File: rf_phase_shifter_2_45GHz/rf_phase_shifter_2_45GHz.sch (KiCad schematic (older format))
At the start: 12 parts, among them J1 Conn_Coaxial, J2 Conn_Coaxial, J3 Conn_Coaxial

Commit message: update
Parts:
- removed FL1: C2327J5003AHF, C2327J5003AHF, symbol RF:C2327J5003AHF
- added FL1: C2327J5003AHF, analog_rf_phase_shifter_module:C2327J5003AHF, symbol analog_rf_phase_shifter_module:C2327J5003AHF
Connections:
- net GND: now also FL1.2 (GND_1), FL1.5 (GND_2)
- net at D1.1 (K), D3.1 (K), L1.2: now also FL1.6 (COUPLED)
- net at D2.1 (K), D4.1 (K), L2.2: now also FL1.4 (DIRECT)
- net at C1.1: now also FL1.1 (INPUT)
- net at C2.2: now also FL1.3 (ISOLATED)
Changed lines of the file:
@@
 EELAYER 30 0
 EELAYER END
-$Descr A4 11693 8268
+$Descr User 8268 5827
 encoding utf-8
 Sheet 1 1
-Title ""
-Date ""
-Rev ""
-Comp ""
+Title "Analog RF phase shifter 2,4-2,5GHz"
+Date "2021-05-03"
+Rev "1.0.0"
+Comp "Marcin Wachowiak, Poland"
 Comment1 ""
 Comment2 ""
@@
 	4450 1950 4450 1900
 Connection ~ 3900 1900
-$Comp
-L RF:C2327J5003AHF FL1
-U 1 1 60586F9C
-P 2200 1700
-F 0 "FL1" H 2950 1965 50  0000 C CNN
-F 1 "C2327J5003AHF" H 2950 1874 50  0000 C CNN
-F 2 "C2327J5003AHF" H 3550 1800 50  0001 L CNN
-F 3 "https://componentsearchengine.com/Datasheets/1/C2327J5003AHF.pdf" H 3550 1700 50  0001 L CNN
-F 4 "Signal Conditioning 2.3-2.7GHz IL=.4dB 3dB 90 Deg." H 3550 1600 50  0001 L CNN "Description"
-F 5 "0.73" H 3550 1500 50  0001 L CNN "Height"
-F 6 "ANAREN" H 3550 1400 50  0001 L CNN "Manufacturer_Name"
-F 7 "C2327J5003AHF" H 3550 1300 50  0001 L CNN "Manufacturer_Part_Number"
-F 8 "620-C2327J5003AHF" H 3550 1200 50  0001 L CNN "Mouser Part Number"
-F 9 "https://www.mouser.com/Search/Refine.aspx?Keyword=620-C2327J5003AHF" H 3550 1100 50  0001 L CNN "Mouser Price/Stock"
-	1    2200 1700
-	1    0    0    -1
-$EndComp
 Wire Wire Line
 	5000 2250 5000 2300
@@
 Wire Notes Line
 	4000 1950 4300 1950
+$Comp
+L analog_rf_phase_shifter_module:C2327J5003AHF FL1
+U 1 1 6090630C
+P 2200 1700
+F 0 "FL1" H 2950 1965 50  0000 C CNN
+F 1 "C2327J5003AHF" H 2950 1874 50  0000 C CNN
+F 2 "analog_rf_phase_shifter_module:C2327J5003AHF" H 3550 1800 50  0001 L CNN
+F 3 "https://componentsearchengine.com/Datasheets/1/C2327J5003AHF.pdf" H 3550 1700 50  0001 L CNN
+F 4 "Signal Conditioning 2.3-2.7GHz IL=.4dB 3dB 90 Deg." H 3550 1600 50  0001 L CNN "Description"
+F 5 "0.73" H 3550 1500 50  0001 L CNN "Height"
+F 6 "ANAREN" H 3550 1400 50  0001 L CNN "Manufacturer_Name"
+F 7 "C2327J5003AHF" H 3550 1300 50  0001 L CNN "Manufacturer_Part_Number"
+	1    2200 1700
+	1    0    0    -1
+$EndComp
 $EndSCHEMATC

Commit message: updated libs
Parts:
- removed J1, J2, J3: Conn_Coaxial, Connector_Coaxial:SMA_Samtec_SMA-J-P-X-ST-EM1_EdgeMount, symbol Connector:Conn_Coaxial
- added J1, J2, J3: CON-SMA-EDGE-S, analog_rf_phase_shifter_module:CON-SMA-EDGE-S, symbol analog_rf_phase_shifter_module:CON-SMA-EDGE-S
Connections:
- net GND: now also J1.2 (Ext), J2.2 (Ext), J3.2 (Ext)
- net at L1.1, L2.1: now also J3.1 (In)
- net at C2.1: now also J2.1 (In)
- net at C1.2: now also J1.1 (In)
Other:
- moved on the sheet: C1, C2, D1, D2, D3, D4, FL1, L1, L2

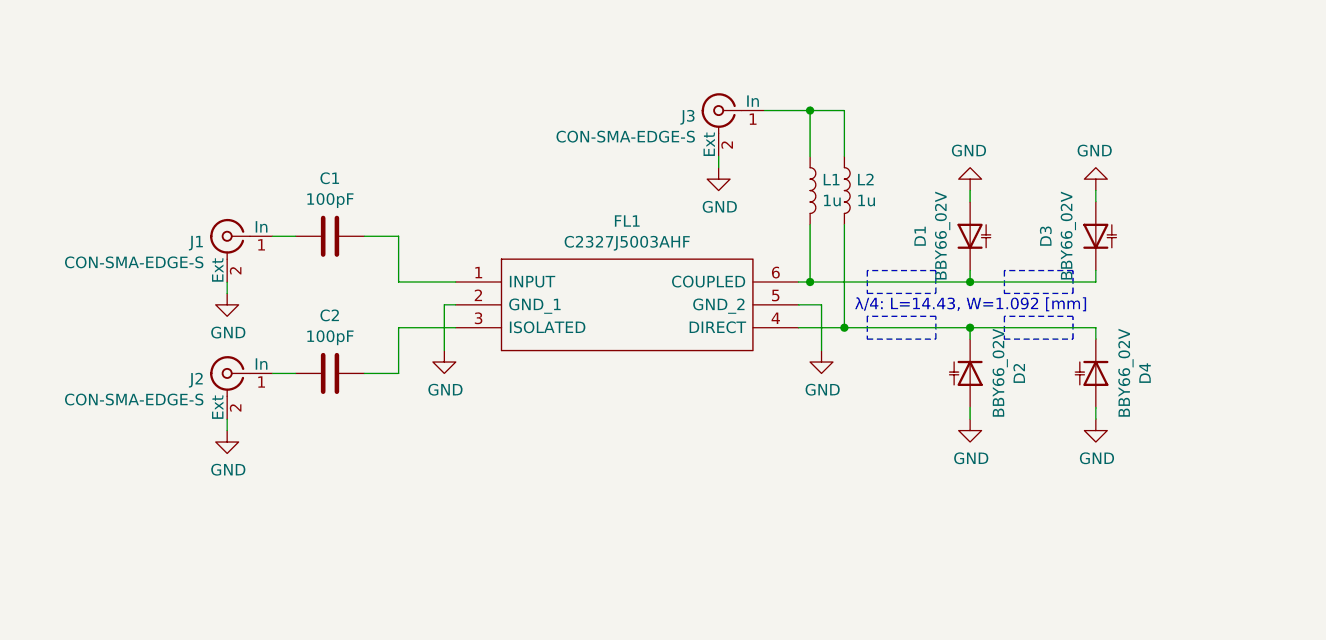
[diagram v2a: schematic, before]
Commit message: pcb init works
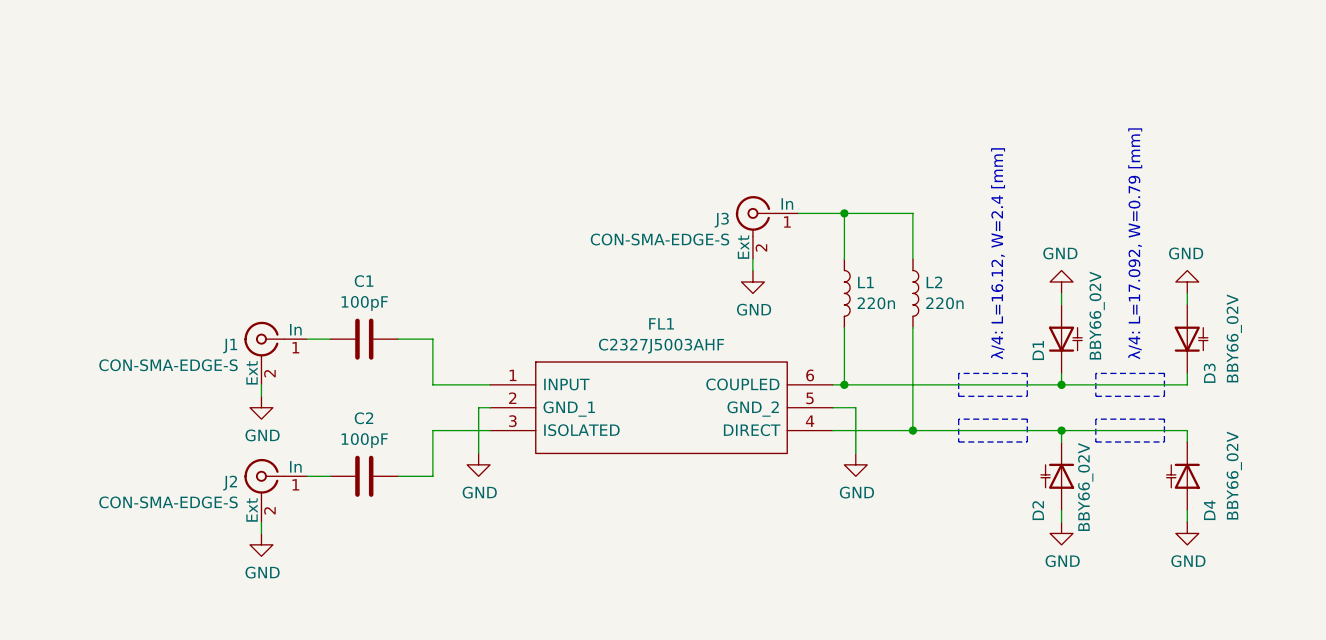
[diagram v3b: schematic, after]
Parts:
- L1, L2: value 1u -> 220n
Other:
- note added: "λ/4: L=16.12, W=2.4 [mm]"
- note added: "λ/4: L=17.092, W=0.79 [mm]"
- note removed: "λ/4: L=14.43, W=1.092 [mm]"
- moved on the sheet: C1, C2, D1, D2, D3, D4, FL1, J1, J2, J3, L1, L2

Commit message: finished pcb layouts
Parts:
- added TL1, TL2: TL_13_2_45GHz, analog_rf_phase_shifter_module:TL_13_2_45GHz, symbol analog_rf_phase_shifter_module:TL_13_2_45GHz
- added TL3, TL4: TL_24_2_45GHz, analog_rf_phase_shifter_module:TL_24_2_45GHz, symbol analog_rf_phase_shifter_module:TL_24_2_45GHz
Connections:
- net at FL1.6 (COUPLED), L1.2: now also TL1.1; no longer D1.1 (K), D3.1 (K)
- net at FL1.4 (DIRECT), L2.2: now also TL2.1; no longer D2.1 (K), D4.1 (K)
- new net: D1.1 (K), TL1.2, TL3.1
- new net: D2.1 (K), TL2.2, TL4.1
- new net: D3.1 (K), TL3.2
- new net: D4.1 (K), TL4.2
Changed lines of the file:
@@
 U 1 1 60376509
 P 5600 2550
-F 0 "D4" H 5750 2650 50  0000 C CNN
-F 1 "BBY66_02V" H 5600 2750 50  0000 C CNN
+F 0 "D4" H 5800 2650 50  0000 C CNN
+F 1 "BBY66_02V" H 5650 2750 50  0000 C CNN
 F 2 "Diode_SMD:D_SOD-523" H 5600 2550 50  0001 C CNN
 F 3 "~" H 5600 2550 50  0001 C CNN
@@
 U 1 1 60375EF1
 P 5600 1950
-F 0 "D3" H 5450 1850 50  0000 C CNN
-F 1 "BBY66_02V" H 5600 1750 50  0000 C CNN
+F 0 "D3" H 5500 1850 50  0000 C CNN
+F 1 "BBY66_02V" H 5650 1750 50  0000 C CNN
 F 2 "Diode_SMD:D_SOD-523" H 5600 1950 50  0001 C CNN
 F 3 "~" H 5600 1950 50  0001 C CNN
@@
 $EndComp
 Wire Wire Line
-	5050 2150 5600 2150
-Wire Wire Line
-	5050 2350 5600 2350
-Wire Wire Line
-	4400 2350 5050 2350
+	5050 2150 5200 2150
+Wire Wire Line
+	5050 2350 5200 2350
+Wire Wire Line
+	4400 2350 4600 2350
 Connection ~ 5050 2150
 Connection ~ 4100 2150
 Wire Wire Line
-	4100 2150 5050 2150
-Text Notes 4800 2050 1    50   ~ 0
+	4100 2150 4600 2150
+Text Notes 4750 2050 1    50   ~ 0
 λ/4: L=16.12, W=2.4 [mm]
 Wire Notes Line
@@
 Wire Wire Line
 	2300 2350 2300 2550
-Text Notes 5400 2050 1    50   ~ 0
+Text Notes 5400 1950 1    50   ~ 0
 λ/4: L=17.092, W=0.79 [mm]
 $Comp
@@
 	1    0    0    -1
 $EndComp
+$Comp
+L analog_rf_phase_shifter_module:TL_13_2_45GHz TL1
+U 1 1 61540646
+P 4750 2100
+F 0 "TL1" H 4500 2100 50  0000 C CNN
+F 1 "TL_13_2_45GHz" V 4850 2450 50  0000 C CNN
+F 2 "analog_rf_phase_shifter_module:TL_13_2_45GHz" H 4500 2250 50  0001 C CNN
+F 3 "" H 4500 2250 50  0001 C CNN
+	1    4750 2100
+	1    0    0    -1
+$EndComp
+Wire Wire Line
+	4900 2150 5050 2150
+$Comp
+L analog_rf_phase_shifter_module:TL_13_2_45GHz TL2
+U 1 1 61540E40
+P 4750 2300
+F 0 "TL2" H 4500 2300 50  0000 C CNN
+F 1 "TL_13_2_45GHz" H 4650 2100 50  0000 C CNN
+F 2 "analog_rf_phase_shifter_module:TL_13_2_45GHz" H 4500 2450 50  0001 C CNN
+F 3 "" H 4500 2450 50  0001 C CNN
+	1    4750 2300
+	1    0    0    -1
+$EndComp
+Wire Wire Line
+	4900 2350 5050 2350
+$Comp
+L analog_rf_phase_shifter_module:TL_24_2_45GHz TL3
+U 1 1 61541F99
+P 5350 2100
+F 0 "TL3" H 5350 2150 50  0000 C CNN
+F 1 "TL_24_2_45GHz" H 5800 2000 50  0000 C CNN
+F 2 "analog_rf_phase_shifter_module:TL_24_2_45GHz" H 5100 2250 50  0001 C CNN
+F 3 "" H 5100 2250 50  0001 C CNN
+	1    5350 2100
+	1    0    0    -1
+$EndComp
+Wire Wire Line
+	5500 2150 5600 2150
+$Comp
+L analog_rf_phase_shifter_module:TL_24_2_45GHz TL4
+U 1 1 615424E1
+P 5350 2300
+F 0 "TL4" H 5350 2150 50  0000 C CNN
+F 1 "TL_24_2_45GHz" H 5800 2300 50  0000 C CNN
+F 2 "analog_rf_phase_shifter_module:TL_24_2_45GHz" H 5100 2450 50  0001 C CNN
+F 3 "" H 5100 2450 50  0001 C CNN
+	1    5350 2300
+	1    0    0    -1
+$EndComp
+Wire Wire Line
+	5500 2350 5600 2350
 $EndSCHEMATC

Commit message: added info about substrate thickness
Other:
- note added: "Substrate: FR4, thickness: 0.6 mm"
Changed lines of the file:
@@
 Wire Wire Line
 	5500 2350 5600 2350
+Text Notes 1475 3175 0    50   ~ 0
+Substrate: FR4, thickness: 0.6 mm
 $EndSCHEMATC

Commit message: Finished layout of second prototypes
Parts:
- D1, D2, D3, D4: value BBY66_02V -> SMV1763-079LF
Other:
- note added: "L=18.75, W=2.4 [mm]"
- note added: "λ/4: L=6.45, W=2.4 [mm]"
- note removed: "λ/4: L=16.12, W=2.4 [mm]"
- note removed: "λ/4: L=17.092, W=0.79 [mm]"
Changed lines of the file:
@@
 P 5050 2750
 F 0 "#PWR0106" H 5050 2500 50  0001 C CNN
-F 1 "GND" H 5055 2577 50  0000 C CNN
+F 1 "GND" H 5050 2575 50  0000 C CNN
 F 2 "" H 5050 2750 50  0001 C CNN
 F 3 "" H 5050 2750 50  0001 C CNN
@@
 U 1 1 60376509
 P 5600 2550
-F 0 "D4" H 5800 2650 50  0000 C CNN
-F 1 "BBY66_02V" H 5650 2750 50  0000 C CNN
+F 0 "D4" H 5525 2650 50  0000 C CNN
+F 1 "SMV1763-079LF " H 5775 2725 50  0000 C CNN
 F 2 "Diode_SMD:D_SOD-523" H 5600 2550 50  0001 C CNN
 F 3 "~" H 5600 2550 50  0001 C CNN
@@
 P 5600 1950
 F 0 "D3" H 5500 1850 50  0000 C CNN
-F 1 "BBY66_02V" H 5650 1750 50  0000 C CNN
+F 1 "SMV1763-079LF " H 5775 1775 50  0000 C CNN
 F 2 "Diode_SMD:D_SOD-523" H 5600 1950 50  0001 C CNN
 F 3 "~" H 5600 1950 50  0001 C CNN
@@
 U 1 1 60375884
 P 5050 2550
-F 0 "D2" H 5200 2450 50  0000 C CNN
-F 1 "BBY66_02V" H 5100 2650 50  0000 C CNN
+F 0 "D2" H 4975 2650 50  0000 C CNN
+F 1 "SMV1763-079LF " H 5225 2725 50  0000 C CNN
 F 2 "Diode_SMD:D_SOD-523" H 5050 2550 50  0001 C CNN
 F 3 "~" H 5050 2550 50  0001 C CNN
@@
 P 5050 1950
 F 0 "D1" H 5000 2050 50  0000 C CNN
-F 1 "BBY66_02V" H 5150 1800 50  0000 C CNN
+F 1 "SMV1763-079LF " H 5300 1800 50  0000 C CNN
 F 2 "Diode_SMD:D_SOD-523" H 5050 1950 50  0001 C CNN
 F 3 "~" H 5050 1950 50  0001 C CNN
@@
 	4100 2150 4600 2150
 Text Notes 4750 2050 1    50   ~ 0
-λ/4: L=16.12, W=2.4 [mm]
+L=18.75, W=2.4 [mm]
 Wire Notes Line
 	4600 2200 4900 2200
@@
 	2300 2350 2300 2550
 Text Notes 5400 1950 1    50   ~ 0
-λ/4: L=17.092, W=0.79 [mm]
+λ/4: L=6.45, W=2.4 [mm]
 $Comp
 L Device:L L1
